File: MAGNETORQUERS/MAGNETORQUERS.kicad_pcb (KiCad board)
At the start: 2 copper layers, 32.4 x 20.2 mm, 13 parts, among them U1 DRV8876PWPR

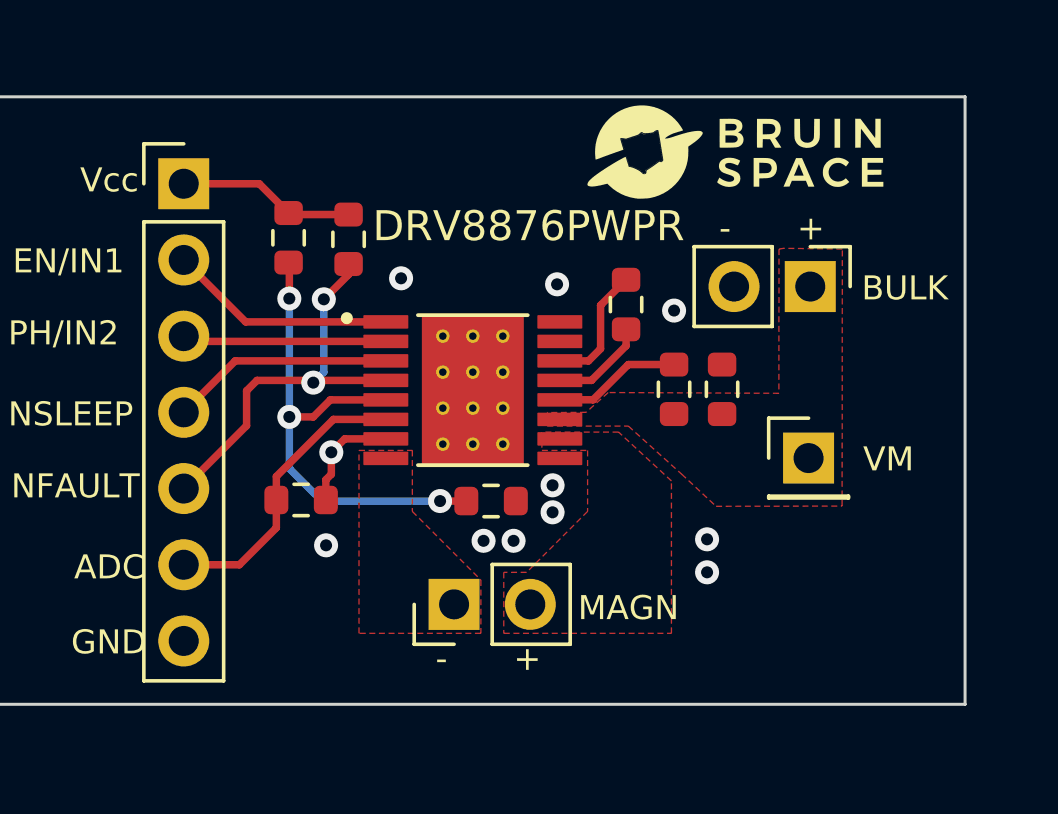
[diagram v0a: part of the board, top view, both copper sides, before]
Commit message: mag pwm control
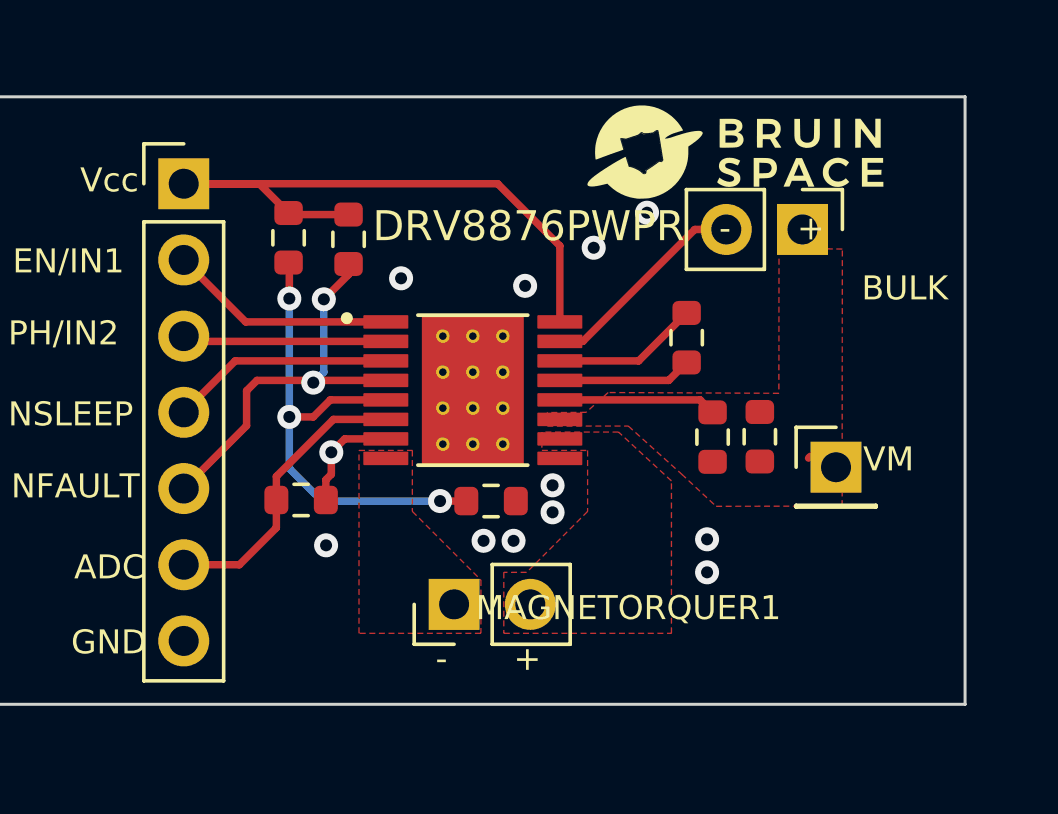
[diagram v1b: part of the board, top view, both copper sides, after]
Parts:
- moved C1 2.30 mm to (147.3, 84.4)
- moved C4 2.05 mm to (148.2, 87.7)
- moved C2 2.02 mm to (149.8, 87.7)
- moved BULKCAP1 1.92 mm to (151.2, 80.8)
- moved VM1 0.96 mm to (152.3, 88.7)
- renumbered 0.022uF to C1, 0.1uF to C2, 0.1uF to C4, MAGN to MAGNETORQUER1, 10k to R1, 16k to REF_1, 50kOhms to REF_2, 2.5kOhms to RIPROPI1, STM to STM1
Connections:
- U1 pad 16: Earth -> Net-(STM1-Vcc)
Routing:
- net Net-(STM1-Vcc): track 5.92 -> 21.8 mm
- net Earth: track 3.68 -> 10.8 mm, vias 11 -> 12
- net Net-(U1-CPH): track 3.24 -> 4.48 mm
- net Net-(U1-VCP): track 4.30 -> 5.27 mm
- net Net-(U1-CPL): track 4.18 -> 4.89 mm

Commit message: hi
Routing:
- net (no net): vias 0 -> 2
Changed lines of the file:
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@@
     (effects (font (size 0.8 0.8) (thickness 0.12)) (justify left bottom))
   )
+  (via (at 100.0252 50.9524) (size 0.8) (drill 0.4) (layers "F.Cu" "B.Cu") (net 0))
+  (via (at 159.0548 71.9836) (size 0.8) (drill 0.4) (layers "F.Cu" "B.Cu") (net 0))
   (segment (start 146.7208 85.803) (end 147.32 85.2038) (width 0.25) (layer "F.Cu") (net 1))
   (segment (start 143.092 85.803) (end 146.7208 85.803) (width 0.25) (layer "F.Cu") (net 1))
@@
   (via (at 137.8 82.4) (size 0.8) (drill 0.4) (layers "F.Cu" "B.Cu") (free) (net 4))
   (via (at 135.3 91.3) (size 0.8) (drill 0.4) (layers "F.Cu" "B.Cu") (free) (net 4))
-  (via (at 142.85 90.2) (size 0.8) (drill 0.4) (layers "F.Cu" "B.Cu") (free) (net 4))
+  (via (at 142.85 90.2) (size 0.8) (drill 0.4) (layers "F.Cu" "B.Cu") (net 4))
   (via (at 144.2212 81.3816) (size 0.8) (drill 0.4) (layers "F.Cu" "B.Cu") (free) (net 4))
   (via (at 135.475 88.2) (size 0.8) (drill 0.4) (layers "F.Cu" "B.Cu") (free) (net 4))
